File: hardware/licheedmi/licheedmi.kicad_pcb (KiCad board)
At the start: 4 copper layers, 94 x 38 mm, 76 parts, among them J1 Conn_01x09, J2 HDMI_A_PCB, J3 LicheePiNano_LCD, J4 HDMI_A, J5 USB_C_Receptacle_USB2.0, U1 TDA19988, U2 LicheeNano, U3 TS3DV20812, U4 SC6206B, U5 CH340C

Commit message: pcb: Fix solder mask clearance and min width
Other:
- rule solder_mask_min_width: 0.15 -> 0.1
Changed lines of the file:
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@@
     (pad_drill 0.762)
     (pad_to_mask_clearance 0.05)
-    (solder_mask_min_width 0.15)
+    (solder_mask_min_width 0.1)
     (aux_axis_origin 0 0)
     (visible_elements 7FFFFFFF)

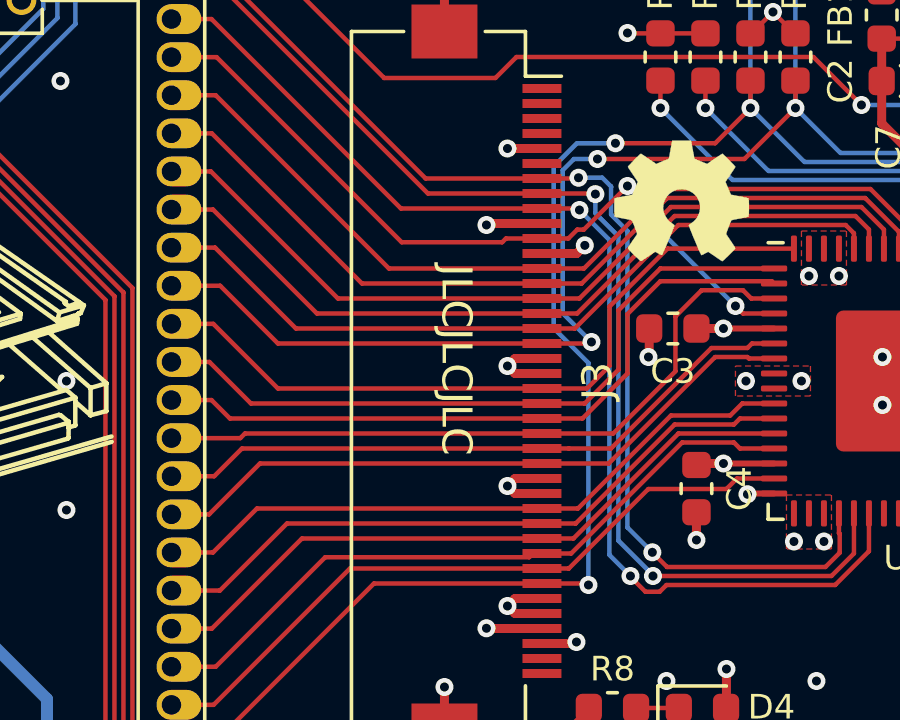
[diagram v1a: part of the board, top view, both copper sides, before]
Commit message: pcb: Fix JLC string
JLCPCB requires the string "JLCJLCJLCJLC" to be specified to control
where they'll put the order number. One of the four JLC was missing...
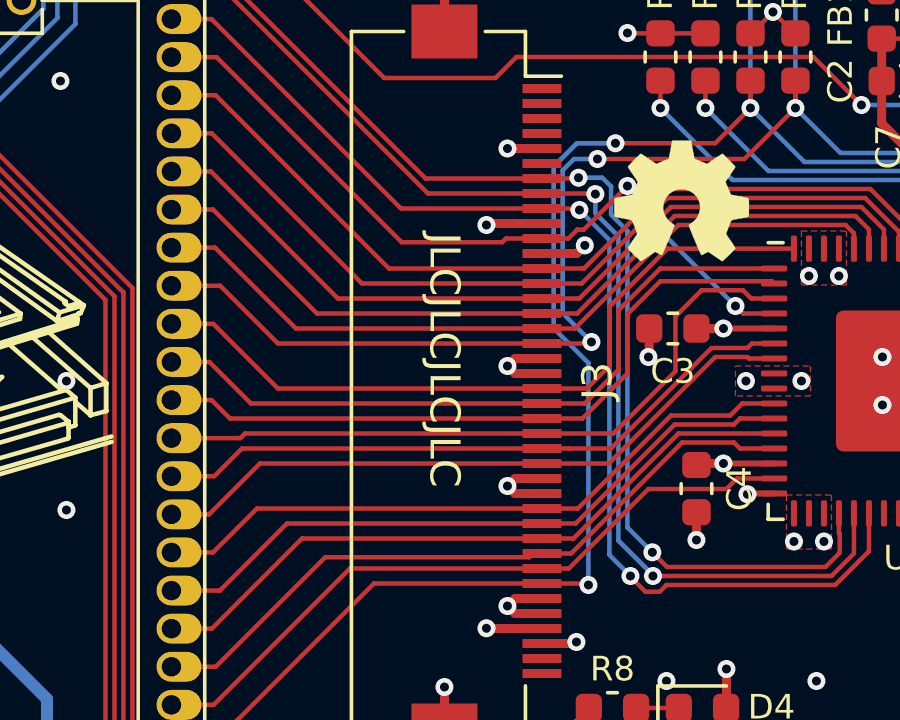
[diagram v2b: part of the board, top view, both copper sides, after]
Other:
- board text added: "JLCJLCJLCJLC"
- board text removed: "JLCJLCJLC"
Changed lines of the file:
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@@
     (effects (font (size 0.82 0.82) (thickness 0.15)))
   )
-  (gr_text JLCJLCJLC (at 118 89.3 270) (layer F.SilkS)
+  (gr_text JLCJLCJLCJLC (at 117.6 89.3 270) (layer F.SilkS)
     (effects (font (size 1 1) (thickness 0.15)))
   )

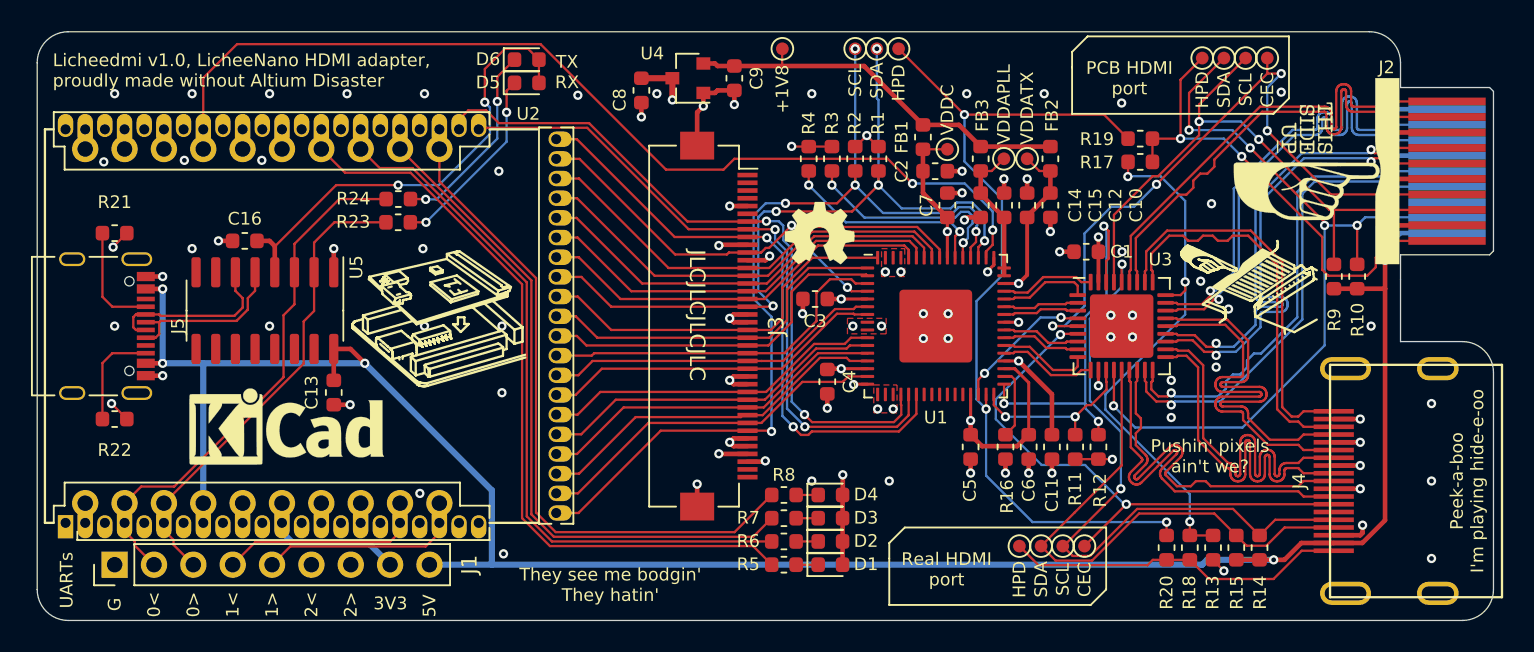
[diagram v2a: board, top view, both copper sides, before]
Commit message: pcb: Wire I2S signals
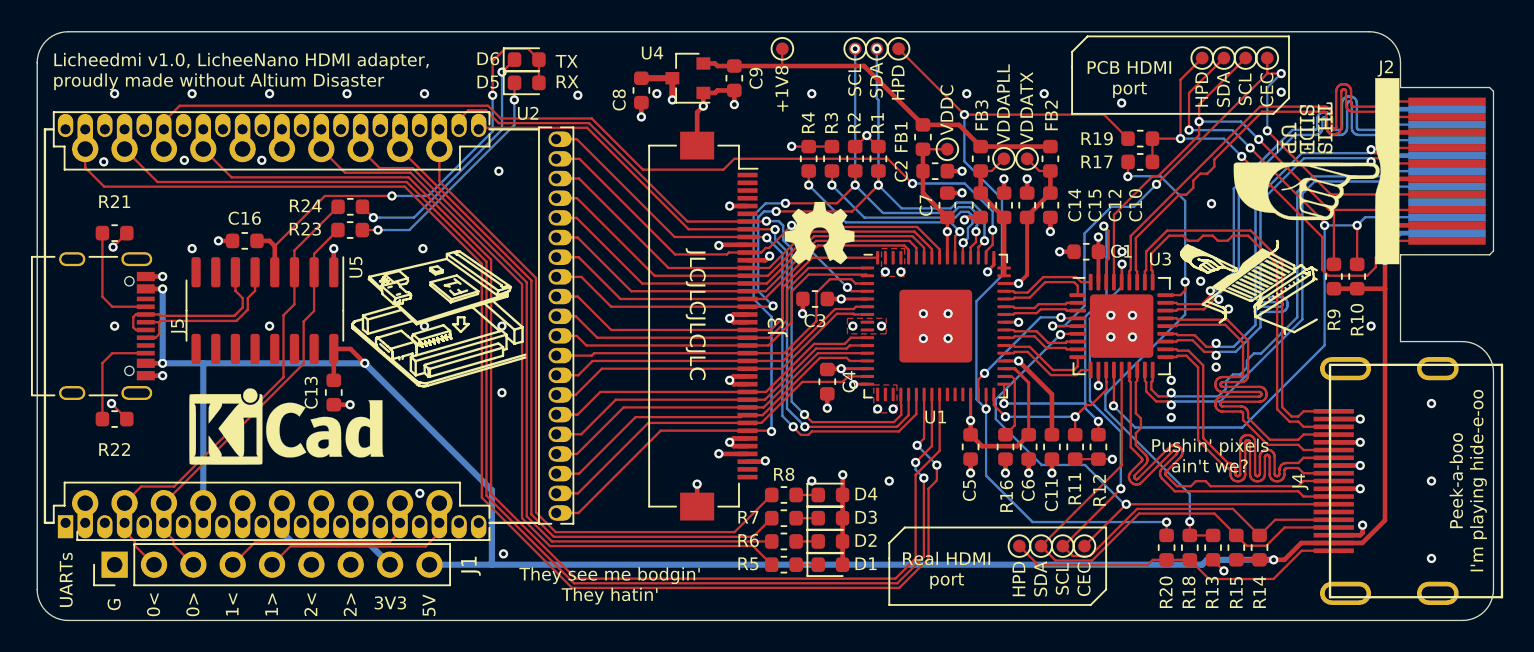
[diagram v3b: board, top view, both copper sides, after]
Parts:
- moved R24 3.14 mm to (95.2, 82.3)
- moved R23 3.14 mm to (95.2, 83.8)
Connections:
- U1 pad 23: Net-(U1-Pad23) -> /I2S_BCLK
- U1 pad 24: Net-(U1-Pad24) -> /I2S_LRCLK
- U1 pad 25: Net-(U1-Pad25) -> /I2S_DO
- U2 pad 57: /HDMI_INT -> /I2S_DO
- U2 pad 59: Net-(U2-Pad59) -> /HDMI_INT
- U2 pad 61: Net-(U2-Pad61) -> /I2S_LRCLK
- U2 pad 63: Net-(U2-Pad63) -> /I2S_BCLK
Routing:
- net /I2S_BCLK: track 0.00 -> 89.3 mm, vias 0 -> 2
- net /I2S_LRCLK: track 0.00 -> 85.2 mm, vias 0 -> 2
- net /I2S_DO: track 0.00 -> 79.4 mm
- net /RX0: track 30.8 -> 27.0 mm
- net Net-(D6-Pad1): track 12.8 -> 16.5 mm
- net /TX0: track 35.0 -> 31.5 mm
- net Net-(D5-Pad1): track 12.4 -> 15.3 mm
- net /HDMI_INT: track 64.7 -> 62.3 mm
- net Net-(U2-Pad63): track 1.27 -> 0.00 mm
- net Net-(U2-Pad61): track 1.27 -> 0.00 mm
- net Net-(U2-Pad59): track 1.27 -> 0.00 mm

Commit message: licheedmi: Release v1.1
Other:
- board text added: "Licheedmi v1.1, LicheeNano HDMI adapter, proudly made without Altium Disaster"
- board text removed: "Licheedmi v1.0, LicheeNano HDMI adapter, proudly made without Altium Disaster"
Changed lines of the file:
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@@
     (effects (font (size 0.82 0.82) (thickness 0.15)))
   )
-  (gr_text "Licheedmi v1.0, LicheeNano HDMI adapter,\nproudly made without Altium Disaster" (at 76 73.5) (layer F.SilkS)
+  (gr_text "Licheedmi v1.1, LicheeNano HDMI adapter,\nproudly made without Altium Disaster" (at 76 73.5) (layer F.SilkS)
     (effects (font (size 0.82 0.82) (thickness 0.15)) (justify left))
   )

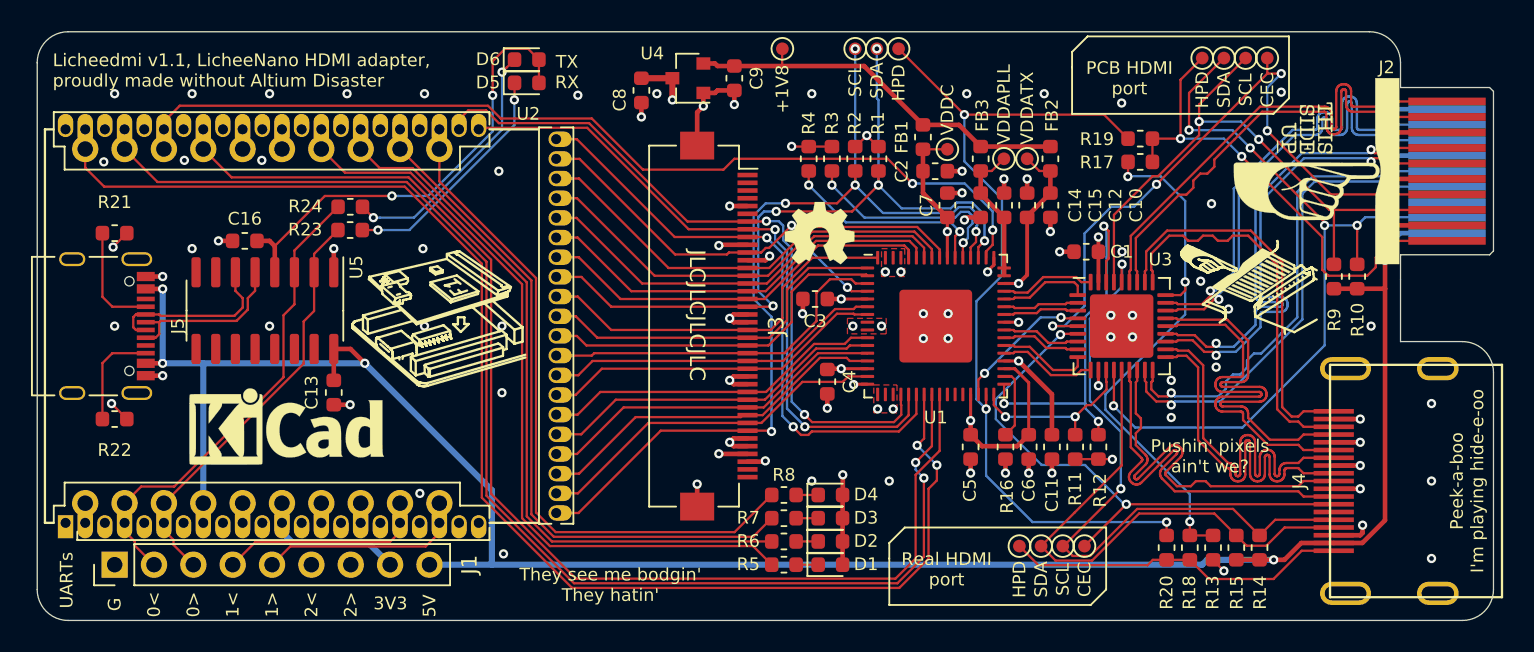
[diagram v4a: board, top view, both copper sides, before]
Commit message: pcb: Route SiI9022A
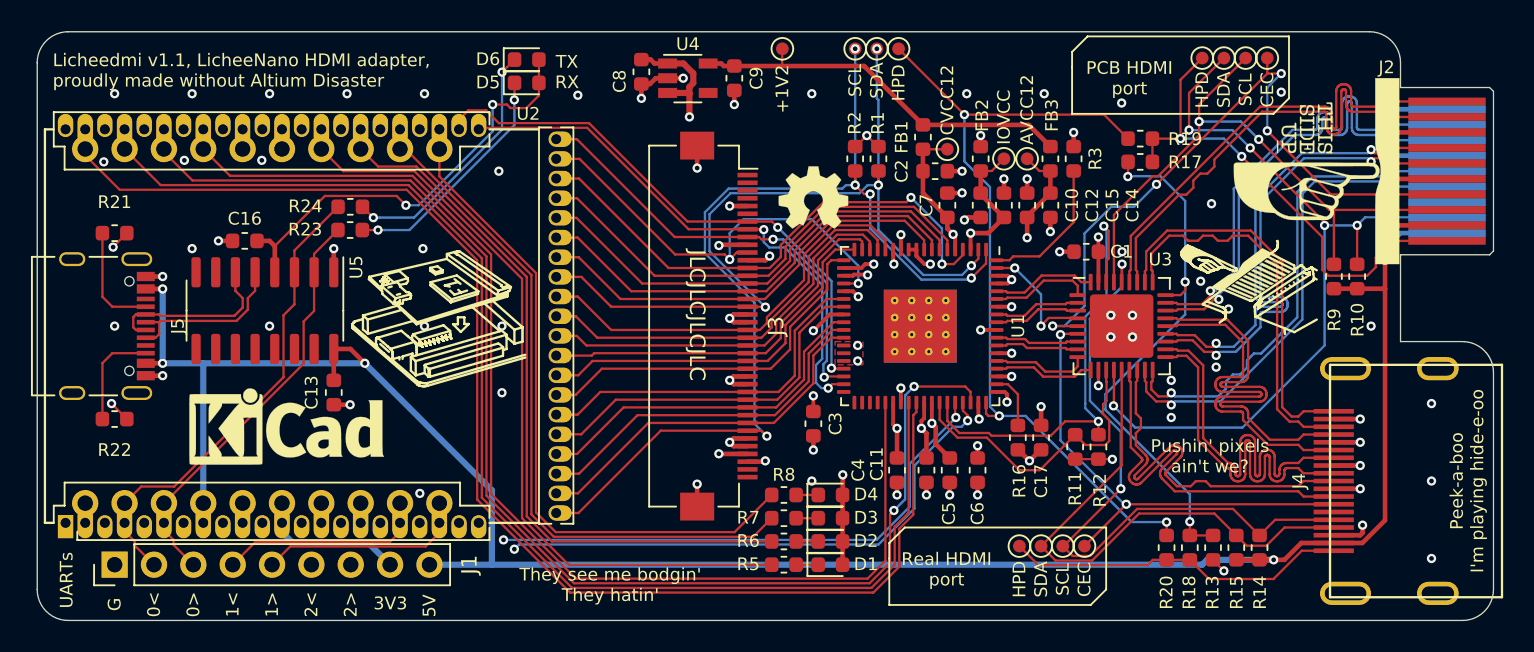
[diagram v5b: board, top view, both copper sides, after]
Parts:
- removed R4: 10k, Resistor_SMD:R_0603_1608Metric
- added C17: 100n, Capacitor_SMD:C_0603_1608Metric, F.Cu at (139.8, 97.2)
- R16: value 10k -> 4k3
- TP12: value VDDC -> CVCC12
- TP13: value +1V8 -> +1V2
- TP14: value VDDATX -> IOVCC
- TP15: value VDDAPLL -> AVCC12
- U1: value TDA19988 -> SiI9022A; footprint Package_DFN_QFN:QFN-64-1EP_9x9mm_P0.5mm_EP4.7x4.7mm -> hdmizness:QFN-72-1EP_10x10mm_P0.5mm_EP4.7x4.7mm_ThermalVias
- U4: value SC6206B -> TLV74312PDBVR; footprint Package_TO_SOT_SMD:SOT-23 -> Package_TO_SOT_SMD:TSOT-23-5
- moved R3 15.6 mm to (141.9, 79.2)
- moved C11 8.24 mm to (132.4, 99.3)
- moved C3 8.05 mm to (125.1, 96.3), turned to 270 degrees
- moved C4 7.27 mm to (130.5, 99.3)
- moved C10 4.50 mm to (135.9, 82.2)
- moved C14 4.50 mm to (140.4, 82.2)
- moved FB2 4.50 mm to (135.9, 79.2)
- moved FB3 4.50 mm to (140.4, 79.2)
- moved C6 3.62 mm to (135.7, 99.3)
- moved REF** 2.33 mm to (125.1, 82.7)
- moved C5 2.02 mm to (133.9, 99.3)
- moved C12 1.50 mm to (137.4, 82.2)
- moved TP14 1.50 mm to (137.4, 79.2)
- moved TP15 1.50 mm to (138.9, 79.2)
- moved C15 1.49 mm to (138.9, 82.2)
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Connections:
- C10 pad 1: /VDDATX -> /IOVCC
- C11 pad 1: /VDDATX -> /IOVCC
- C12 pad 1: /VDDATX -> /IOVCC
- C14 pad 1: /VDDAPLL -> /AVCC12
- C15 pad 1: /VDDAPLL -> /AVCC12
- C2 pad 1: /VDDA -> /CVCC12
- C3 pad 1: /VDDA -> /CVCC12
- C4 pad 1: /VDDA -> /CVCC12
- C5 pad 1: /VDDA -> /CVCC12
- C6 pad 1: /VDDA -> /CVCC12
- C7 pad 1: /VDDA -> /CVCC12
- C9 pad 1: +1V8 -> +1V2
- FB1 pad 1: /VDDA -> /CVCC12
- FB1 pad 2: +1V8 -> +1V2
- FB2 pad 1: /VDDATX -> /IOVCC
- FB2 pad 2: +1V8 -> +3V3
- FB3 pad 1: /VDDAPLL -> /AVCC12
- FB3 pad 2: +1V8 -> +1V2
- TP12 pad 1: /VDDA -> /CVCC12
- TP13 pad 1: +1V8 -> +1V2
- TP14 pad 1: /VDDATX -> /IOVCC
- TP15 pad 1: /VDDAPLL -> /AVCC12
- U1 pad 1: /LCD_G6 -> /CPU_SCL
- U1 pad 10: /LCD_R7 -> GND
- U1 pad 11: /LCD_R6 -> GND
- U1 pad 12: /LCD_R5 -> /CVCC12
- U1 pad 13: /LCD_R4 -> GND
- U1 pad 14: /VDDA -> /LCD_G7
- U1 pad 15: /LCD_R3 -> /LCD_G6
- U1 pad 16: GND -> /LCD_G5
- U1 pad 17: GND -> /LCD_G4
- U1 pad 18: GND -> /LCD_G3
- U1 pad 19: GND -> /LCD_G2
- U1 pad 2: /LCD_G5 -> /CPU_SDA
- U1 pad 20: /LCD_DE -> GND
- U1 pad 21: /LCD_VSYNC -> /IOVCC
- U1 pad 22: /LCD_HSYNC -> /LCD_CLK
- U1 pad 23: /I2S_BCLK -> GND
- U1 pad 24: /I2S_LRCLK -> /LCD_R7
- U1 pad 25: /I2S_DO -> /LCD_R6
- U1 pad 26: Net-(U1-Pad26) -> /CVCC12
- U1 pad 27: Net-(U1-Pad27) -> /LCD_R5
- U1 pad 28: Net-(U1-Pad28) -> /LCD_R4
- U1 pad 29: /VDDA -> /LCD_R3
- U1 pad 3: /LCD_G4 -> /IOVCC
- U1 pad 30: /HDCEC -> GND
- U1 pad 31: /HPD -> GND
- U1 pad 32: /HDSDA -> GND
- U1 pad 33: /HDSCL -> /LCD_DE
- U1 pad 34: Net-(R16-Pad1) -> /LCD_HSYNC
- U1 pad 35: /VDDA -> /LCD_VSYNC
- U1 pad 36: /VDDATX -> Net-(U1-Pad36)
- U1 pad 37: /HDC_N -> Net-(U1-Pad37)
- U1 pad 38: /HDC_P -> Net-(U1-Pad38)
- U1 pad 39: /HD0_N -> Net-(U1-Pad39)
- U1 pad 4: /LCD_CLK -> /LCD_B7
- U1 pad 40: /HD0_P -> Net-(U1-Pad40)
- U1 pad 41: /VDDATX -> /I2S_DO
- U1 pad 42: /HD1_N -> /CVCC12
- U1 pad 43: /HD1_P -> GND
- U1 pad 44: /HD2_N -> /I2S_LRCLK
- U1 pad 45: /HD2_P -> /I2S_BCLK
- U1 pad 46: /VDDATX -> /IOVCC
- U1 pad 47: /VDDAPLL -> /CVCC12
- U1 pad 48: /VDDAPLL -> /HDSDA
- U1 pad 49: GND -> /HDSCL
- U1 pad 5: /VDDA -> /CVCC12
- U1 pad 50: /HDMI_INT -> /HDMI_CDC
- U1 pad 51: /CPU_SDA -> /HDMI_~RST
- U1 pad 52: /CPU_SCL -> /HDMI_INT
- U1 pad 53: Net-(R3-Pad2) -> /CVCC12
- U1 pad 54: Net-(R4-Pad2) -> /HPD
- U1 pad 55: /VDDA -> GND
- U1 pad 56: /LCD_B7 -> Net-(R16-Pad1)
- U1 pad 57: /LCD_B6 -> GND
- U1 pad 58: /LCD_B5 -> /HDC_N
- U1 pad 59: /LCD_B4 -> /HDC_P
- U1 pad 6: /LCD_G3 -> /LCD_B6
- U1 pad 60: /LCD_B3 -> /AVCC12
- U1 pad 61: GND -> /HD0_N
- U1 pad 62: GND -> /HD0_P
- U1 pad 64: /LCD_G7 -> /HD1_N
- U1 pad 65: GND -> /HD1_P
- U1 pad 7: /LCD_G2 -> /LCD_B5
- U1 pad 8: GND -> /LCD_B4
- U1 pad 9: GND -> /LCD_B3
- U2 pad 16: Net-(U2-Pad16) -> /HDMI_~RST
- U2 pad 2: Net-(U2-Pad2) -> /HDMI_CDC
- U4 pad 1: GND -> +3V3
- U4 pad 2: +1V8 -> GND
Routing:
- net /HDMI_CDC: track 0.00 -> 65.6 mm, vias 0 -> 2
- net /CVCC12: track 0.00 -> 54.8 mm, vias 0 -> 8
- net /VDDA: track 51.7 -> 0.00 mm, vias 4 -> 0
- net /HDMI_~RST: track 0.00 -> 47.8 mm, vias 0 -> 2
- net /IOVCC: track 0.00 -> 34.0 mm, vias 0 -> 3
- net +1V8: track 25.7 -> 0.00 mm
- net +1V2: track 0.00 -> 25.4 mm
- net /HDMI_INT: track 62.3 -> 86.0 mm
- net /VDDATX: track 23.4 -> 0.00 mm, vias 3 -> 0
- net /AVCC12: track 0.00 -> 22.0 mm, vias 0 -> 4
- net Net-(R4-Pad2): track 13.7 -> 0.00 mm, vias 2 -> 0
- net /LCD_HSYNC: track 39.1 -> 28.8 mm
- net /LCD_DE: track 45.6 -> 35.9 mm
- net /VDDAPLL: track 9.22 -> 0.00 mm
- net /LCD_VSYNC: track 43.8 -> 35.4 mm
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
